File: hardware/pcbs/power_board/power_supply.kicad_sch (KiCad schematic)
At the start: 30 parts, among them J15 PJ-102AH, J16 ScrewTerminal_02, J17 ScrewTerminal_02, J18 ScrewTerminal_02, J19 ScrewTerminal_02, J20 ScrewTerminal_02, J21 Header_02x04, U12 LMR38020, U13 LMR38020

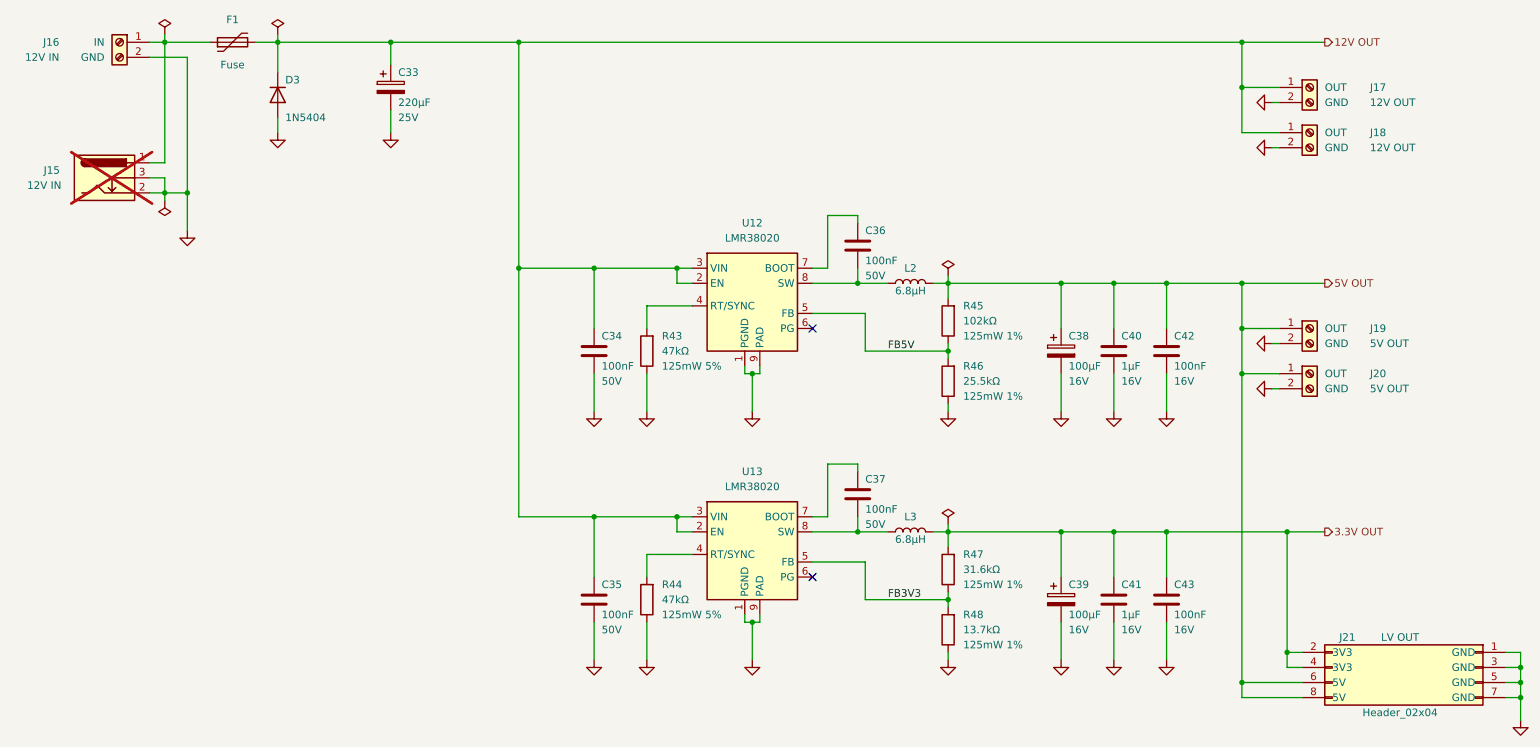
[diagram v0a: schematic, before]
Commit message: power_board: finalise isolated chargers and place USB3 passthrough
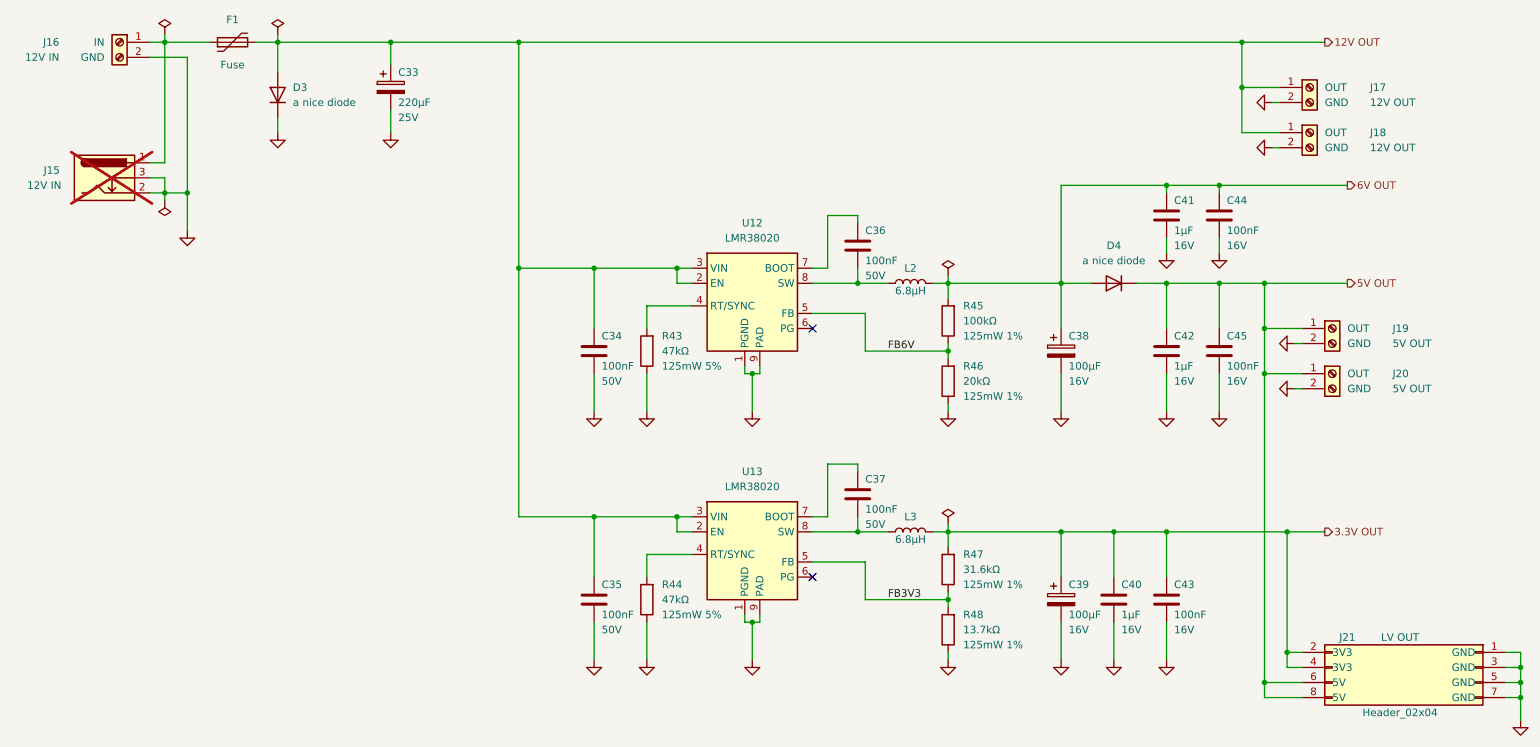
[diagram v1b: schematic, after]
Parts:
- removed D3: 1N5404, Diode_THT:D_DO-201AD_P15.24mm_Horizontal, symbol Diode:1N5404
- added C41: 1μF, Capacitor_SMD:C_0805_2012Metric, symbol Device:C
- added C44: 100nF, Capacitor_SMD:C_0805_2012Metric, symbol Device:C
- added D3, D4: a nice diode, Diode_SMD:D_SMC, symbol Diode:1N4007
- C39: footprint Capacitor_THT:CP_Radial_D5.0mm_P2.00mm -> Capacitor_SMD:CP_Elec_6.3x5.4; Shop https://store.comet.bg/Catalogue/Product/3785/ -> https://store.comet.bg/Catalogue/Product/29563/
- R45: value 102kΩ -> 100kΩ; Shop https://eu.mouser.com/ProductDetail/Bourns/CR0805-FX-1023EL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 -> TODO
- R46: value 25.5kΩ -> 20kΩ; Shop https://eu.mouser.com/ProductDetail/Bourns/CR0805-FX-2552EL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 -> TODO
- renumbered C41 to C40, C40 to C42, C42 to C45
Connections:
- net 12V OUT: now also D3.2 (A)
- net 5V OUT: now also D4.1 (K); no longer C38.1, L2.2, R45.2
- net GND: now also C41.2, C44.2, D3.1 (K)
- net FB5V renamed FB6V
- new net 6V OUT: C38.1, C41.1, C44.1, D4.2 (A), L2.2, R45.2
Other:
- moved on the sheet: C42, C45, J19, J20

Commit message: power_board: arrange stuff on board
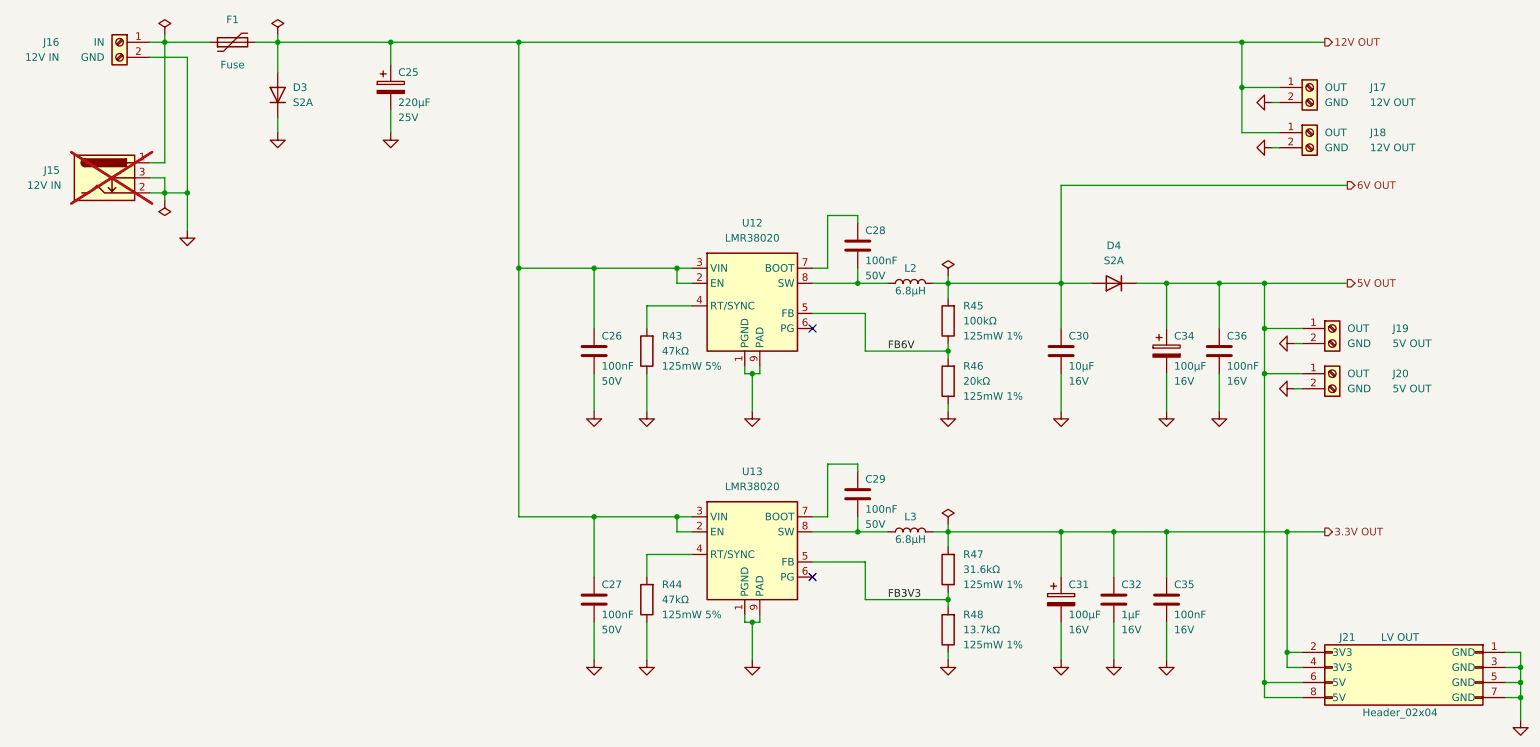
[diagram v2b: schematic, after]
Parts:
- removed C41, C42: 1μF, Capacitor_SMD:C_0805_2012Metric, symbol Device:C
- removed C44: 100nF, Capacitor_SMD:C_0805_2012Metric, symbol Device:C
- added C30: 10μF, Capacitor_SMD:C_0805_2012Metric, symbol Device:C
- D3, D4: value a nice diode -> S2A; footprint Diode_SMD:D_SMC -> Diode_SMD:D_SMB; Shop TODO -> https://store.comet.bg/Catalogue/Product/48275/
- renumbered C33 to C25, C34 to C26, C35 to C27, C36 to C28, C37 to C29, C39 to C31, C40 to C32, C38 to C34, C43 to C35, C45 to C36
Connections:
- net 5V OUT: now also C34.1
- net 6V OUT: now also C30.1; no longer C34.1
- net GND: now also C30.2
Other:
- moved on the sheet: C34

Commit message: power_board: finalise silkscreen
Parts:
- J17, J18: Purpose Pin1 OUT -> 12V
- J19, J20: Purpose Pin1 OUT -> 5V
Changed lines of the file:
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@@
 			)
 		)
-		(property "Purpose Pin1" "OUT"
+		(property "Purpose Pin1" "5V"
 			(at 245.11 86.36 0)
 			(effects
@@
 			)
 		)
-		(property "Purpose Pin1" "OUT"
+		(property "Purpose Pin1" "5V"
 			(at 245.11 93.98 0)
 			(effects
@@
 			)
 		)
-		(property "Purpose Pin1" "OUT"
+		(property "Purpose Pin1" "12V"
 			(at 241.3 53.34 0)
 			(effects
@@
 			)
 		)
-		(property "Purpose Pin1" "OUT"
+		(property "Purpose Pin1" "12V"
 			(at 241.3 45.72 0)
 			(effects

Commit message: power_board: some fixes in bom
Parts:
- R45: Shop TODO -> https://store.comet.bg/Catalogue/Product/24862/
- R46: Shop TODO -> https://store.comet.bg/Catalogue/Product/29761/
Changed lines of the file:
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@@
 			)
 		)
-		(property "Shop" "TODO"
+		(property "Shop" "https://store.comet.bg/Catalogue/Product/29761/"
 			(at 177.8 95.25 0)
 			(effects
@@
 			)
 		)
-		(property "Shop" "TODO"
+		(property "Shop" "https://store.comet.bg/Catalogue/Product/24862/"
 			(at 177.8 85.09 0)
 			(effects

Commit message: power_board: final version
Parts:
- C26, C27, C28, C29, C35, C36: LCSC (none) -> C49678
- C30: LCSC (none) -> C15850
- C32: LCSC (none) -> C28323
- D3, D4: LCSC (none) -> C7420368
- L2, L3: LCSC (none) -> C222938
- R43, R44: LCSC (none) -> C17713
- R45: LCSC (none) -> C149504
- R46: LCSC (none) -> C4328
- R47: LCSC (none) -> C17623
- R48: LCSC (none) -> C17448
- U12, U13: LCSC (none) -> C5149193
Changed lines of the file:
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@@
 			)
 		)
+		(property "LCSC" "C222938"
+			(at 171.45 78.74 0)
+			(effects
+				(font
+					(size 1.27 1.27)
+				)
+				(hide yes)
+			)
+		)
 		(pin "1"
 		)
@@
 			)
 		)
+		(property "LCSC" "C49678"
+			(at 214.63 132.08 0)
+			(effects
+				(font
+					(size 1.27 1.27)
+				)
+				(hide yes)
+			)
+		)
 		(pin "1"
 		)
@@
 			)
 		)
+		(property "LCSC" "C222938"
+			(at 171.45 120.65 0)
+			(effects
+				(font
+					(size 1.27 1.27)
+				)
+				(hide yes)
+			)
+		)
 		(pin "1"
 		)
@@
 			)
 		)
+		(property "LCSC" "C28323"
+			(at 205.74 132.08 0)
+			(effects
+				(font
+					(size 1.27 1.27)
+				)
+				(hide yes)
+			)
+		)
 		(pin "1"
 		)
@@
 			)
 		)
+		(property "LCSC" "C49678"
+			(at 118.11 132.08 0)
+			(effects
+				(font
+					(size 1.27 1.27)
+				)
+				(hide yes)
+			)
+		)
 		(pin "1"
 		)
@@
 			)
 		)
+		(property "LCSC" "C17623"
+			(at 177.8 127 0)
+			(effects
+				(font
+					(size 1.27 1.27)
+				)
+				(hide yes)
+			)
+		)
 		(pin "1"
 		)
@@
 			)
 		)
+		(property "LCSC" "C5149193"
+			(at 144.78 123.19 0)
+			(effects
+				(font
+					(size 1.27 1.27)
+				)
+				(hide yes)
+			)
+		)
 		(pin "1"
 		)
@@
 			)
 		)
+		(property "LCSC" "C49678"
+			(at 162.56 72.39 0)
+			(effects
+				(font
+					(size 1.27 1.27)
+				)
+				(hide yes)
+			)
+		)
 		(pin "1"
 		)
@@
 			)
 		)
+		(property "LCSC" "C49678"
+			(at 118.11 90.17 0)
+			(effects
+				(font
+					(size 1.27 1.27)
+				)
+				(hide yes)
+			)
+		)
 		(pin "1"
 		)
@@
 			)
 		)
+		(property "LCSC" "C7420368"
+			(at 205.74 78.74 0)
+			(effects
+				(font
+					(size 1.27 1.27)
+				)
+				(hide yes)
+			)
+		)
 		(pin "2"
 		)
@@
 			)
 		)
+		(property "LCSC" "C49678"
+			(at 162.56 114.3 0)
+			(effects
+				(font
+					(size 1.27 1.27)
+				)
+				(hide yes)
+			)
+		)
 		(pin "1"
 		)
@@
 			)
 		)
+		(property "LCSC" "C5149193"
+			(at 144.78 81.28 0)
+			(effects
+				(font
+					(size 1.27 1.27)
+				)
+				(hide yes)
+			)
+		)
 		(pin "1"
 		)
@@
 			)
 		)
+		(property "LCSC" "C49678"
+			(at 223.52 90.17 0)
+			(effects
+				(font
+					(size 1.27 1.27)
+				)
+				(hide yes)
+			)
+		)
 		(pin "1"
 		)
@@
 			)
 		)
+		(property "LCSC" "C4328"
+			(at 177.8 95.25 0)
+			(effects
+				(font
+					(size 1.27 1.27)
+				)
+				(hide yes)
+			)
+		)
 		(pin "1"
 		)
@@
 			)
 		)
+		(property "LCSC" "C17448"
+			(at 177.8 137.16 0)
+			(effects
+				(font
+					(size 1.27 1.27)
+				)
+				(hide yes)
+			)
+		)
 		(pin "1"
 		)
@@
 			)
 		)
+		(property "LCSC" "C17713"
+			(at 127 90.17 0)
+			(effects
+				(font
+					(size 1.27 1.27)
+				)
+				(hide yes)
+			)
+		)
 		(pin "1"
 		)
@@
 			)
 		)
+		(property "LCSC" "C149504"
+			(at 177.8 85.09 0)
+			(effects
+				(font
+					(size 1.27 1.27)
+				)
+				(hide yes)
+			)
+		)
 		(pin "1"
 		)
@@
 			)
 		)
+		(property "LCSC" "C17713"
+			(at 127 132.08 0)
+			(effects
+				(font
+					(size 1.27 1.27)
+				)
+				(hide yes)
+			)
+		)
 		(pin "1"
 		)
@@
 			)
 		)
+		(property "LCSC" "C15850"
+			(at 196.85 90.17 0)
+			(effects
+				(font
+					(size 1.27 1.27)
+				)
+				(hide yes)
+			)
+		)
 		(pin "1"
 		)
@@
 			(at 64.77 46.99 0)
 			(effects
+				(font
+					(size 1.27 1.27)
+				)
+				(hide yes)
+			)
+		)
+		(property "LCSC" "C7420368"
+			(at 64.77 46.99 0)
+			(effects

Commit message: power_board: some extra fixes
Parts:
- U12, U13: footprint Package_SO:Texas_R-PDSO-G8_EP2.95x4.9mm_Mask2.4x3.1mm -> ics:Texas_R-PDSO-G8_EP2.95x4.9mm_Mask2.4x3.1mm_ThermalVias
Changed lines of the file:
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@@
 			)
 		)
-		(property "Footprint" "Package_SO:Texas_R-PDSO-G8_EP2.95x4.9mm_Mask2.4x3.1mm"
+		(property "Footprint" "ics:Texas_R-PDSO-G8_EP2.95x4.9mm_Mask2.4x3.1mm_ThermalVias"
 			(at 144.78 143.51 0)
 			(effects
@@
 			)
 		)
-		(property "Footprint" "Package_SO:Texas_R-PDSO-G8_EP2.95x4.9mm_Mask2.4x3.1mm"
+		(property "Footprint" "ics:Texas_R-PDSO-G8_EP2.95x4.9mm_Mask2.4x3.1mm_ThermalVias"
 			(at 144.78 101.6 0)
 			(effects

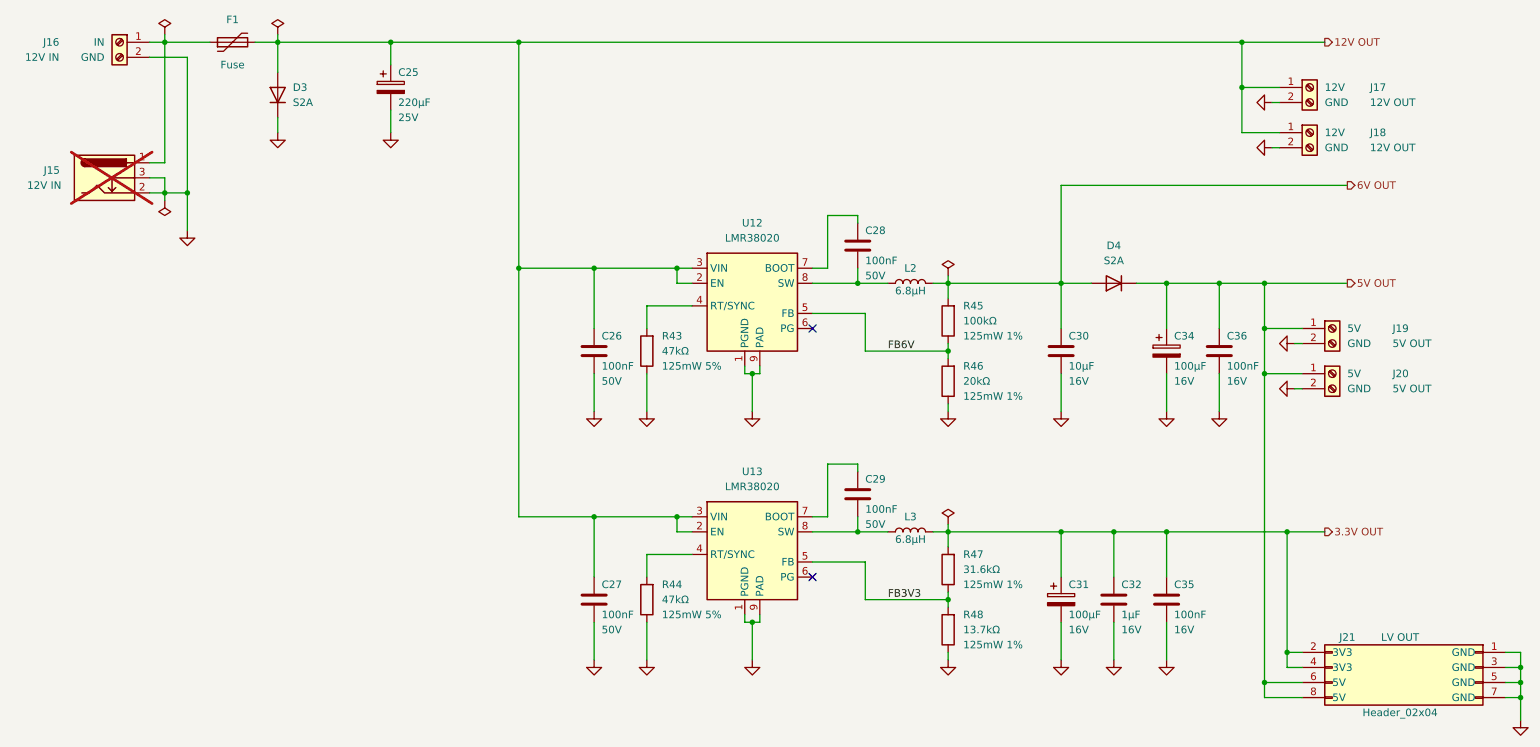
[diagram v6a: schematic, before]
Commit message: power_board: nuke general purpose leds and power cycler
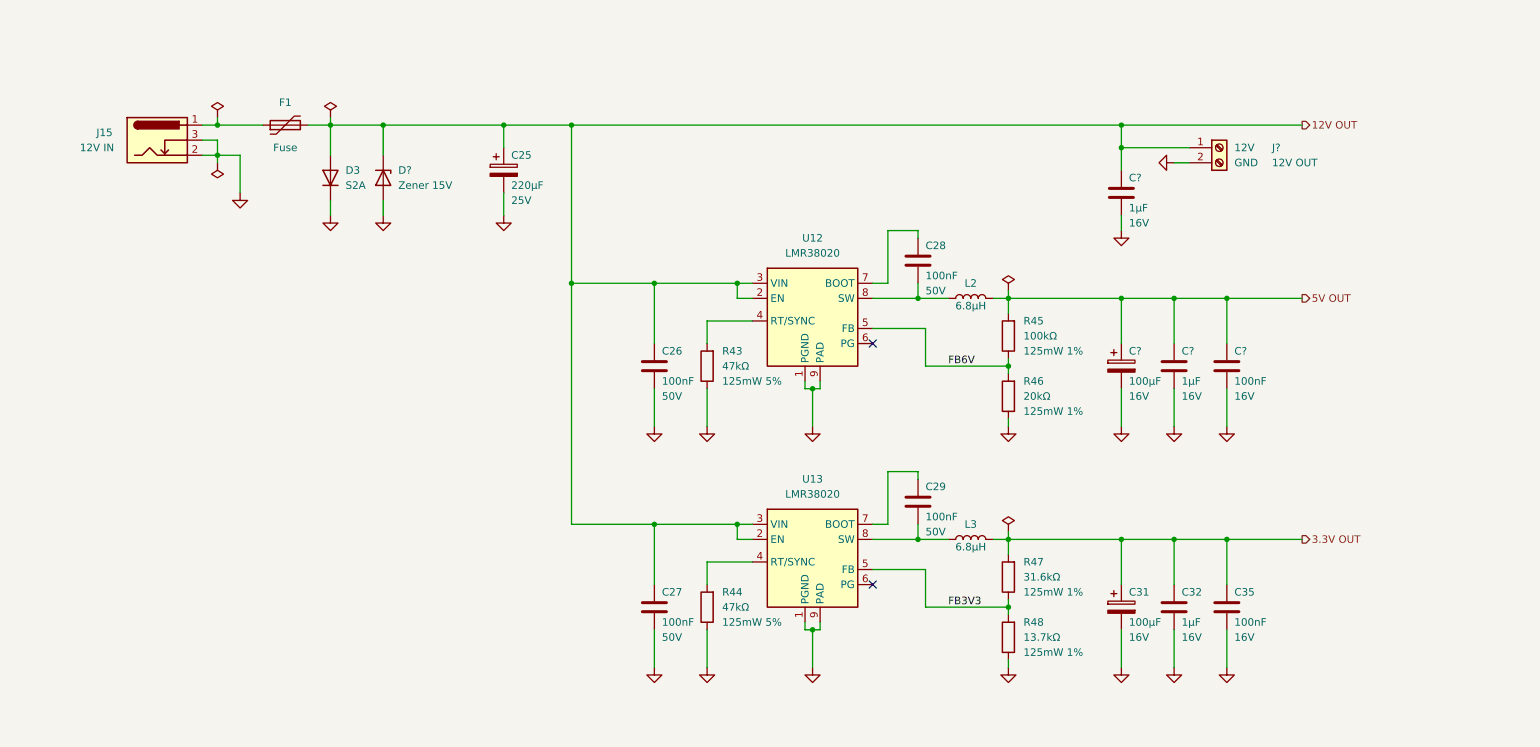
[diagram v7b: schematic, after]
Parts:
- removed C30: 10μF, Capacitor_SMD:C_0805_2012Metric, symbol Device:C
- removed C34: 100μF, Capacitor_SMD:CP_Elec_6.3x5.4, symbol Device:C_Polarized
- removed C36: 100nF, Capacitor_SMD:C_0805_2012Metric, symbol Device:C
- removed D4: S2A, Diode_SMD:D_SMB, symbol Diode:1N4007
- removed J16, J17, J18, J19, J20: ScrewTerminal_02, conn:TerminalBlock_4Ucon_1x02_P3.50mm_Vertical, symbol conn:Screw_Terminal_01x02
- removed J21: Header_02x04, conn:PinHeader_2x04_P2.54mm_Vertical, symbol conn:Conn_02x04_Odd_Even
- added C?: 100μF, Capacitor_THT:CP_Radial_D5.0mm_P2.00mm, symbol Device:C_Polarized
- added C? (x2): 1μF, Capacitor_SMD:C_0805_2012Metric, symbol Device:C
- added C?: 100nF, Capacitor_SMD:C_0805_2012Metric, symbol Device:C
- added D?: Zener 15V, Diode_SMD:D_SMB, symbol Device:D_Zener
- added J?: ScrewTerminal_02, conn:TerminalBlock_4Ucon_1x02_P3.50mm_Vertical, symbol conn:Screw_Terminal_01x02
- C25: footprint Capacitor_SMD:CP_Elec_8x10.5 -> Capacitor_THT:CP_Radial_D6.3mm_P2.50mm; Part (none) -> RK1E221M-RBE11; Shop https://store.comet.bg/Catalogue/Product/7420/ -> https://store.comet.bg/Catalogue/Product/3792/
- C31: footprint Capacitor_SMD:CP_Elec_6.3x5.4 -> Capacitor_THT:CP_Radial_D5.0mm_P2.00mm; Part (none) -> RK1C101M-RBD11; Shop https://store.comet.bg/Catalogue/Product/29563/ -> https://store.comet.bg/Catalogue/Product/3785/
- J15: now fitted
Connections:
- net 6V OUT is gone; now on net 5V OUT: L2.2, R45.2
- net 12V OUT: now also C?.1, D?.1 (K), J?.1 (Pin_1)
- net 5V OUT: now also C?.1, C?.1, C?.1
- net GND: now also C?.2, C?.2, C?.2, C?.2, D?.2 (A), J?.2 (Pin_2)
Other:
- moved on the sheet: C25, C26, C27, C28, C29, C31, C32, C35, D3, F1, L2, L3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
